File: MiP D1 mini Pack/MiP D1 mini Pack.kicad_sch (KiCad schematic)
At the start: 4 parts, among them J3 Debug, U1 WEMOS_D1_mini

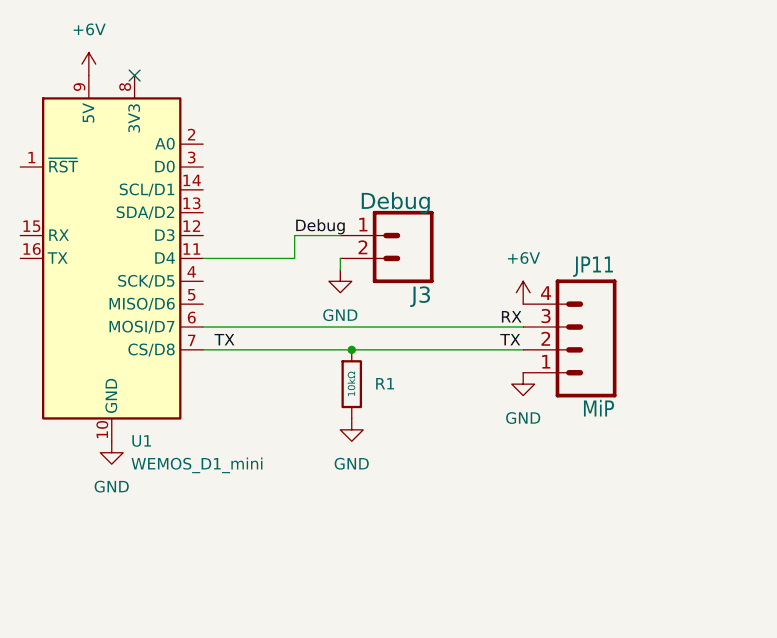
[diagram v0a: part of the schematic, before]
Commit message: Schematic cleanup
Renamed the connector references to account for the lost J1 and J2 from the v2 board.  Moved things around a bit.
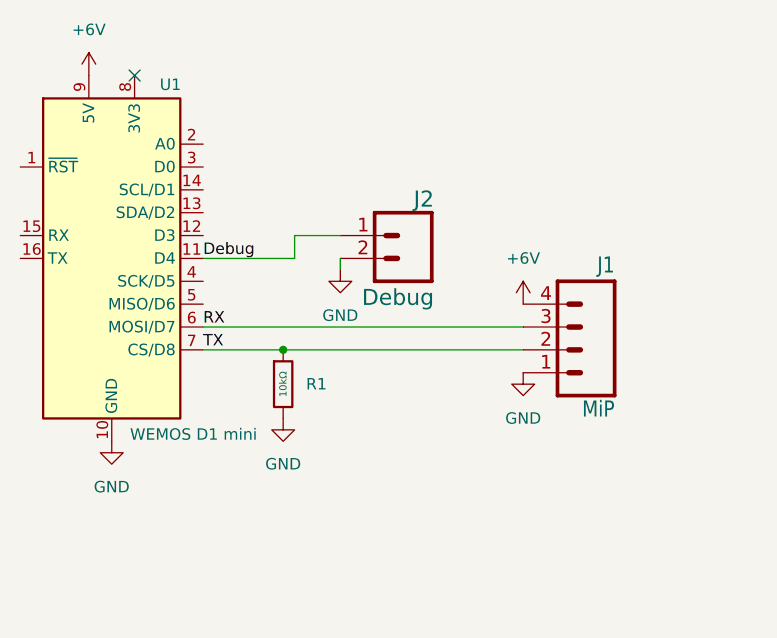
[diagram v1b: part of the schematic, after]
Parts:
- U1: value WEMOS_D1_mini -> WEMOS D1 mini
- renumbered JP11 to J1, J3 to J2
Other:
- moved on the sheet: R1
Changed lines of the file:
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@@
 	)
 	(junction
-		(at 158.75 116.84)
+		(at 151.13 116.84)
 		(diameter 0)
 		(color 0 0 0 0)
@@
 	(wire
 		(pts
-			(xy 142.24 116.84) (xy 158.75 116.84)
+			(xy 151.13 116.84) (xy 177.8 116.84)
 		)
 		(stroke
@@
 	(wire
 		(pts
+			(xy 142.24 116.84) (xy 151.13 116.84)
+		)
+		(stroke
+			(width 0)
+			(type default)
+		)
+	)
+	(wire
+		(pts
 			(xy 152.4 104.14) (xy 157.48 104.14)
 		)
@@
 	(wire
 		(pts
-			(xy 158.75 116.84) (xy 177.8 116.84)
+			(xy 152.4 104.14) (xy 152.4 106.68)
+		)
+		(stroke
+			(width 0.1524)
+			(type solid)
+		)
+	)
+	(wire
+		(pts
+			(xy 142.24 106.68) (xy 152.4 106.68)
 		)
 		(stroke
@@
 	(wire
 		(pts
-			(xy 152.4 104.14) (xy 152.4 106.68)
-		)
-		(stroke
-			(width 0.1524)
-			(type solid)
-		)
-	)
-	(wire
-		(pts
-			(xy 142.24 106.68) (xy 152.4 106.68)
+			(xy 157.48 106.68) (xy 157.48 107.95)
 		)
 		(stroke
@@
 	(wire
 		(pts
-			(xy 157.48 106.68) (xy 157.48 107.95)
+			(xy 142.24 114.3) (xy 177.8 114.3)
 		)
 		(stroke
 			(width 0)
 			(type default)
-		)
-	)
-	(wire
-		(pts
-			(xy 142.24 114.3) (xy 177.8 114.3)
-		)
-		(stroke
-			(width 0)
-			(type default)
-		)
-	)
-	(label "RX"
-		(at 175.26 114.3 0)
-		(effects
-			(font
-				(size 1.27 1.27)
-			)
-			(justify left bottom)
 		)
 	)
@@
 		)
 	)
-	(label "TX"
-		(at 175.26 116.84 0)
+	(label "RX"
+		(at 142.24 114.3 0)
 		(effects
 			(font
@@
 		)
 	)
-	(label "TX"
-		(at 143.51 116.84 0)
+	(label "Debug"
+		(at 142.24 106.68 0)
 		(effects
 			(font
@@
 		)
 	)
-	(label "Debug"
-		(at 152.4 104.14 0)
+	(label "TX"
+		(at 142.24 116.84 0)
 		(effects
 			(font
@@
 		(in_pos_files yes)
 		(dnp no)
-		(property "Reference" "JP11"
+		(property "Reference" "J1"
 			(at 187.96 108.458 0)
 			(show_name no)
@@
 			(project "MiP D1 mini Pack"
 				(path "/b2e24b55-e9ec-47a9-a18b-15b59863e31a"
-					(reference "JP11")
+					(reference "J1")
 					(unit 1)
 				)
@@
 		(in_pos_files yes)
 		(dnp no)
-		(property "Reference" "J3"
-			(at 167.64 109.728 0)
+		(property "Reference" "J2"
+			(at 167.894 99.06 0)
 			(show_name no)
 			(do_not_autoplace no)
@@
 		)
 		(property "Value" "Debug"
-			(at 167.64 99.314 0)
+			(at 167.894 109.982 0)
 			(show_name no)
 			(do_not_autoplace no)
@@
 			(project "MiP D1 mini Pack"
 				(path "/b2e24b55-e9ec-47a9-a18b-15b59863e31a"
-					(reference "J3")
+					(reference "J2")
 					(unit 1)
 				)
@@
 	(symbol
 		(lib_id "PCM_JLCPCB-Resistors:0402,10kΩ")
-		(at 158.75 120.65 0)
+		(at 151.13 120.65 0)
 		(unit 1)
 		(body_style 1)
@@
 		(fields_autoplaced yes)
 		(property "Reference" "R1"
-			(at 161.29 120.6499 0)
+			(at 153.67 120.6499 0)
 			(show_name no)
 			(do_not_autoplace no)
@@
 		)
 		(property "Value" "10kΩ"
-			(at 158.75 120.65 90)
+			(at 151.13 120.65 90)
 			(show_name no)
 			(do_not_autoplace yes)
@@
 		)
 		(property "Footprint" "Resistor_SMD:R_0805_2012Metric_Pad1.20x1.40mm_HandSolder"
-			(at 156.972 120.65 90)
+			(at 149.352 120.65 90)
 			(hide yes)
 			(show_name no)
@@
 		)
 		(property "Datasheet" "https://www.lcsc.com/datasheet/lcsc_datasheet_2411221126_UNI-ROYAL-Uniroyal-Elec-0402WGF1002TCE_C25744.pdf"
-			(at 158.75 120.65 0)
+			(at 151.13 120.65 0)
 			(hide yes)
 			(show_name no)
@@
 		)
 		(property "Description" "62.5mW Thick Film Resistors 50V ±100ppm/°C ±1% 10kΩ 0402 Chip Resistor - Surface Mount ROHS"
-			(at 158.75 120.65 0)
+			(at 151.13 120.65 0)
 			(hide yes)
 			(show_name no)
@@
 		)
 		(property "LCSC" "C25744"
-			(at 158.75 120.65 0)
+			(at 151.13 120.65 0)
 			(hide yes)
 			(show_name no)
@@
 		)
 		(property "Stock" "24372091"
-			(at 158.75 120.65 0)
+			(at 151.13 120.65 0)
 			(hide yes)
 			(show_name no)
@@
 		)
 		(property "Price" "0.004USD"
-			(at 158.75 120.65 0)
+			(at 151.13 120.65 0)
 			(hide yes)
 			(show_name no)
@@
 		)
 		(property "Process" "SMT"
-			(at 158.75 120.65 0)
+			(at 151.13 120.65 0)
 			(hide yes)
 			(show_name no)
@@
 		)
 		(property "Minimum Qty" "20"
-			(at 158.75 120.65 0)
+			(at 151.13 120.65 0)
 			(hide yes)
 			(show_name no)
@@
 		)
 		(property "Attrition Qty" "10"
-			(at 158.75 120.65 0)
+			(at 151.13 120.65 0)
 			(hide yes)
 			(show_name no)
@@
 		)
 		(property "Class" "Basic Component"
-			(at 158.75 120.65 0)
+			(at 151.13 120.65 0)
 			(hide yes)
 			(show_name no)
@@
 		)
 		(property "Category" "Resistors,Chip Resistor - Surface Mount"
-			(at 158.75 120.65 0)
+			(at 151.13 120.65 0)
 			(hide yes)
 			(show_name no)
@@
 		)
 		(property "Manufacturer" "UNI-ROYAL(Uniroyal Elec)"
-			(at 158.75 120.65 0)
+			(at 151.13 120.65 0)
 			(hide yes)
 			(show_name no)
@@
 		)
 		(property "Part" "0402WGF1002TCE"
-			(at 158.75 120.65 0)
+			(at 151.13 120.65 0)
 			(hide yes)
 			(show_name no)
@@
 		)
 		(property "Resistance" "10kΩ"
-			(at 158.75 120.65 0)
+			(at 151.13 120.65 0)
 			(hide yes)
 			(show_name no)
@@
 		)
 		(property "Power(Watts)" "62.5mW"
-			(at 158.75 120.65 0)
+			(at 151.13 120.65 0)
 			(hide yes)
 			(show_name no)
@@
 		)
 		(property "Type" "Thick Film Resistors"
-			(at 158.75 120.65 0)
+			(at 151.13 120.65 0)
 			(hide yes)
 			(show_name no)
@@
 		)
 		(property "Overload Voltage (Max)" "50V"
-			(at 158.75 120.65 0)
+			(at 151.13 120.65 0)
 			(hide yes)
 			(show_name no)
@@
 		)
 		(property "Operating Temperature Range" "-55°C~+155°C"
-			(at 158.75 120.65 0)
+			(at 151.13 120.65 0)
 			(hide yes)
 			(show_name no)
@@
 		)
 		(property "Tolerance" "±1%"
-			(at 158.75 120.65 0)
+			(at 151.13 120.65 0)
 			(hide yes)
 			(show_name no)
@@
 		)
 		(property "Temperature Coefficient" "±100ppm/°C"
-			(at 158.75 120.65 0)
+			(at 151.13 120.65 0)
 			(hide yes)
 			(show_name no)
@@
 	(symbol
 		(lib_id "power:GND")
-		(at 158.75 124.46 0)
+		(at 151.13 124.46 0)
 		(unit 1)
 		(body_style 1)
@@
 		(fields_autoplaced yes)
 		(property "Reference" "#PWR06"
-			(at 158.75 130.81 0)
+			(at 151.13 130.81 0)
 			(hide yes)
 			(show_name no)
@@
 		)
 		(property "Value" "GND"
-			(at 158.75 129.54 0)
+			(at 151.13 129.54 0)
 			(show_name no)
 			(do_not_autoplace no)
@@
 		)
 		(property "Footprint" ""
-			(at 158.75 124.46 0)
+			(at 151.13 124.46 0)
 			(hide yes)
 			(show_name no)
@@
 		)
 		(property "Datasheet" ""
-			(at 158.75 124.46 0)
+			(at 151.13 124.46 0)
 			(hide yes)
 			(show_name no)
@@
 		)
 		(property "Description" "Power symbol creates a global label with name \"GND\" , ground"
-			(at 158.75 124.46 0)
+			(at 151.13 124.46 0)
 			(hide yes)
 			(show_name no)
@@
 		(in_pos_files yes)
 		(dnp no)
-		(fields_autoplaced yes)
 		(property "Reference" "U1"
-			(at 134.2233 127 0)
+			(at 137.414 87.376 0)
 			(show_name no)
 			(do_not_autoplace no)
@@
 			)
 		)
-		(property "Value" "WEMOS_D1_mini"
-			(at 134.2233 129.54 0)
-			(show_name no)
-			(do_not_autoplace no)
+		(property "Value" "WEMOS D1 mini"
+			(at 134.112 126.238 0)
+			(show_name no)
+			(do_not_autoplace no)
